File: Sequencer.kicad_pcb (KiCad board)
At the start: 4 copper layers, 100.6 x 100 mm, 230 parts, among them J1 Conn_02x03_Odd_Even, J2 Conn_02x05_Odd_Even, J3 Conn_02x03_Odd_Even, J4 Conn_01x03, Q1 BC847, Q2 BC847, Q3 BC847, Q4 BC847, SW1 SW_Push, SW10 SW_SPDT_MSM, SW11 SW_SPDT_MSM, SW12 SW_SPDT_MSM, SW2 SW_SPDT_MSM, SW3 SW_SPDT_MSM, SW4 SW_SPDT_MSM, SW5 SW_SPDT_MSM, SW6 SW_SPDT_MSM, SW7 SW_SPDT, SW8 SW_SPDT, SW9 SW_SPDT_MSM, U1 L7805, U10 TL072, U11 74AHCT1G125, U12 TL072, U13 74AHCT1G125, U14 TL072, U2 ATmega328PB-AU, U3 74AHCT1G125, U4 MCP6002-xMS, U5 MCP6002-xMS, U6 MCP6002-xMS, U7 MCP6002-xMS, U8 TL072, U9 74AHCT1G125, X1 20MHz

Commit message: Branding.
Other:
- board text added: "+12V"
- board text added: "-12V"
- board text added: "I2C"
- board text added: "ICSP"
- board text added: "Marangisto 2018"
- board text added: "Modular Sequencer"
- board text added: "Rev A"
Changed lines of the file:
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@@
   (general
     (thickness 1.6)
-    (drawings 88)
+    (drawings 96)
     (tracks 1658)
     (zones 0)
@@
     (descr "Through hole straight pin header, 2x03, 2.54mm pitch, double rows")
     (tags "Through hole pin header THT 2x03 2.54mm double row")
-    (fp_text reference J1 (at 1.27 2.33) (layer B.SilkS)
+    (fp_text reference J1 (at 1.26956 -7.36602) (layer B.SilkS)
       (effects (font (size 0.75 1) (thickness 0.15)) (justify mirror))
     )
@@
       (effects (font (size 0.75 1) (thickness 0.15)) (justify mirror))
     )
+    (fp_line (start 0 1.27) (end 3.81 1.27) (layer B.Fab) (width 0.1))
+    (fp_line (start 3.81 1.27) (end 3.81 -6.35) (layer B.Fab) (width 0.1))
+    (fp_line (start 3.81 -6.35) (end -1.27 -6.35) (layer B.Fab) (width 0.1))
+    (fp_line (start -1.27 -6.35) (end -1.27 0) (layer B.Fab) (width 0.1))
+    (fp_line (start -1.27 0) (end 0 1.27) (layer B.Fab) (width 0.1))
+    (fp_line (start -1.33 -6.41) (end 3.87 -6.41) (layer B.SilkS) (width 0.12))
+    (fp_line (start -1.33 -1.27) (end -1.33 -6.41) (layer B.SilkS) (width 0.12))
+    (fp_line (start 3.87 1.33) (end 3.87 -6.41) (layer B.SilkS) (width 0.12))
+    (fp_line (start -1.33 -1.27) (end 1.27 -1.27) (layer B.SilkS) (width 0.12))
+    (fp_line (start 1.27 -1.27) (end 1.27 1.33) (layer B.SilkS) (width 0.12))
+    (fp_line (start 1.27 1.33) (end 3.87 1.33) (layer B.SilkS) (width 0.12))
+    (fp_line (start -1.33 0) (end -1.33 1.33) (layer B.SilkS) (width 0.12))
+    (fp_line (start -1.33 1.33) (end 0 1.33) (layer B.SilkS) (width 0.12))
+    (fp_line (start -1.8 1.8) (end -1.8 -6.85) (layer B.CrtYd) (width 0.05))
+    (fp_line (start -1.8 -6.85) (end 4.35 -6.85) (layer B.CrtYd) (width 0.05))
+    (fp_line (start 4.35 -6.85) (end 4.35 1.8) (layer B.CrtYd) (width 0.05))
+    (fp_line (start 4.35 1.8) (end -1.8 1.8) (layer B.CrtYd) (width 0.05))
     (fp_text user %R (at 1.27 -2.54 -90) (layer B.Fab)
       (effects (font (size 1 1) (thickness 0.15)) (justify mirror))
     )
-    (fp_line (start 4.35 1.8) (end -1.8 1.8) (layer B.CrtYd) (width 0.05))
-    (fp_line (start 4.35 -6.85) (end 4.35 1.8) (layer B.CrtYd) (width 0.05))
-    (fp_line (start -1.8 -6.85) (end 4.35 -6.85) (layer B.CrtYd) (width 0.05))
-    (fp_line (start -1.8 1.8) (end -1.8 -6.85) (layer B.CrtYd) (width 0.05))
-    (fp_line (start -1.33 1.33) (end 0 1.33) (layer B.SilkS) (width 0.12))
-    (fp_line (start -1.33 0) (end -1.33 1.33) (layer B.SilkS) (width 0.12))
-    (fp_line (start 1.27 1.33) (end 3.87 1.33) (layer B.SilkS) (width 0.12))
-    (fp_line (start 1.27 -1.27) (end 1.27 1.33) (layer B.SilkS) (width 0.12))
-    (fp_line (start -1.33 -1.27) (end 1.27 -1.27) (layer B.SilkS) (width 0.12))
-    (fp_line (start 3.87 1.33) (end 3.87 -6.41) (layer B.SilkS) (width 0.12))
-    (fp_line (start -1.33 -1.27) (end -1.33 -6.41) (layer B.SilkS) (width 0.12))
-    (fp_line (start -1.33 -6.41) (end 3.87 -6.41) (layer B.SilkS) (width 0.12))
-    (fp_line (start -1.27 0) (end 0 1.27) (layer B.Fab) (width 0.1))
-    (fp_line (start -1.27 -6.35) (end -1.27 0) (layer B.Fab) (width 0.1))
-    (fp_line (start 3.81 -6.35) (end -1.27 -6.35) (layer B.Fab) (width 0.1))
-    (fp_line (start 3.81 1.27) (end 3.81 -6.35) (layer B.Fab) (width 0.1))
-    (fp_line (start 0 1.27) (end 3.81 1.27) (layer B.Fab) (width 0.1))
-    (pad 6 thru_hole oval (at 2.54 -5.08) (size 1.7 1.7) (drill 1) (layers *.Cu *.Mask)
-      (net 3 +5V))
-    (pad 5 thru_hole oval (at 0 -5.08) (size 1.7 1.7) (drill 1) (layers *.Cu *.Mask)
-      (net 3 +5V))
-    (pad 4 thru_hole oval (at 2.54 -2.54) (size 1.7 1.7) (drill 1) (layers *.Cu *.Mask)
-      (net 43 SCL))
-    (pad 3 thru_hole oval (at 0 -2.54) (size 1.7 1.7) (drill 1) (layers *.Cu *.Mask)
-      (net 42 SDA))
-    (pad 2 thru_hole oval (at 2.54 0) (size 1.7 1.7) (drill 1) (layers *.Cu *.Mask)
-      (net 149 GND))
     (pad 1 thru_hole rect (at 0 0) (size 1.7 1.7) (drill 1) (layers *.Cu *.Mask)
       (net 149 GND))
+    (pad 2 thru_hole oval (at 2.54 0) (size 1.7 1.7) (drill 1) (layers *.Cu *.Mask)
+      (net 149 GND))
+    (pad 3 thru_hole oval (at 0 -2.54) (size 1.7 1.7) (drill 1) (layers *.Cu *.Mask)
+      (net 42 SDA))
+    (pad 4 thru_hole oval (at 2.54 -2.54) (size 1.7 1.7) (drill 1) (layers *.Cu *.Mask)
+      (net 43 SCL))
+    (pad 5 thru_hole oval (at 0 -5.08) (size 1.7 1.7) (drill 1) (layers *.Cu *.Mask)
+      (net 3 +5V))
+    (pad 6 thru_hole oval (at 2.54 -5.08) (size 1.7 1.7) (drill 1) (layers *.Cu *.Mask)
+      (net 3 +5V))
     (model ${KISYS3DMOD}/Connector_PinHeader_2.54mm.3dshapes/PinHeader_2x03_P2.54mm_Vertical.wrl
       (at (xyz 0 0 0))
@@
     )
   )
+  (gr_text ICSP (at 157.64256 153.39568) (layer B.SilkS)
+    (effects (font (size 1 1.5) (thickness 0.2)) (justify mirror))
+  )
+  (gr_text I2C (at 118.14556 72.49668) (layer B.SilkS)
+    (effects (font (size 1 1.5) (thickness 0.2)) (justify mirror))
+  )
+  (gr_text "+12V\n\n" (at 184.05856 59.92368) (layer B.SilkS)
+    (effects (font (size 1 1) (thickness 0.25)) (justify mirror))
+  )
+  (gr_text "-12V\n\n" (at 173.89856 69.95668) (layer B.SilkS)
+    (effects (font (size 1 1) (thickness 0.25)) (justify mirror))
+  )
+  (gr_line (start 181.13756 71.22668) (end 176.81956 71.22668) (layer B.SilkS) (width 0.4))
+  (gr_text "Rev A" (at 196.63156 100.43668 90) (layer B.SilkS)
+    (effects (font (size 1.5 1.5) (thickness 0.3)) (justify mirror))
+  )
+  (gr_text "Marangisto 2018" (at 196.63156 66.52768 90) (layer B.SilkS)
+    (effects (font (size 1.5 1.5) (thickness 0.3)) (justify mirror))
+  )
+  (gr_text "Modular  Sequencer" (at 101.63556 87.86368 90) (layer B.SilkS)
+    (effects (font (size 4 3.5) (thickness 0.3)) (justify mirror))
+  )
   (gr_line (start 198.8011 155.0036) (end 198.8011 55.0036) (layer Edge.Cuts) (width 0.2))

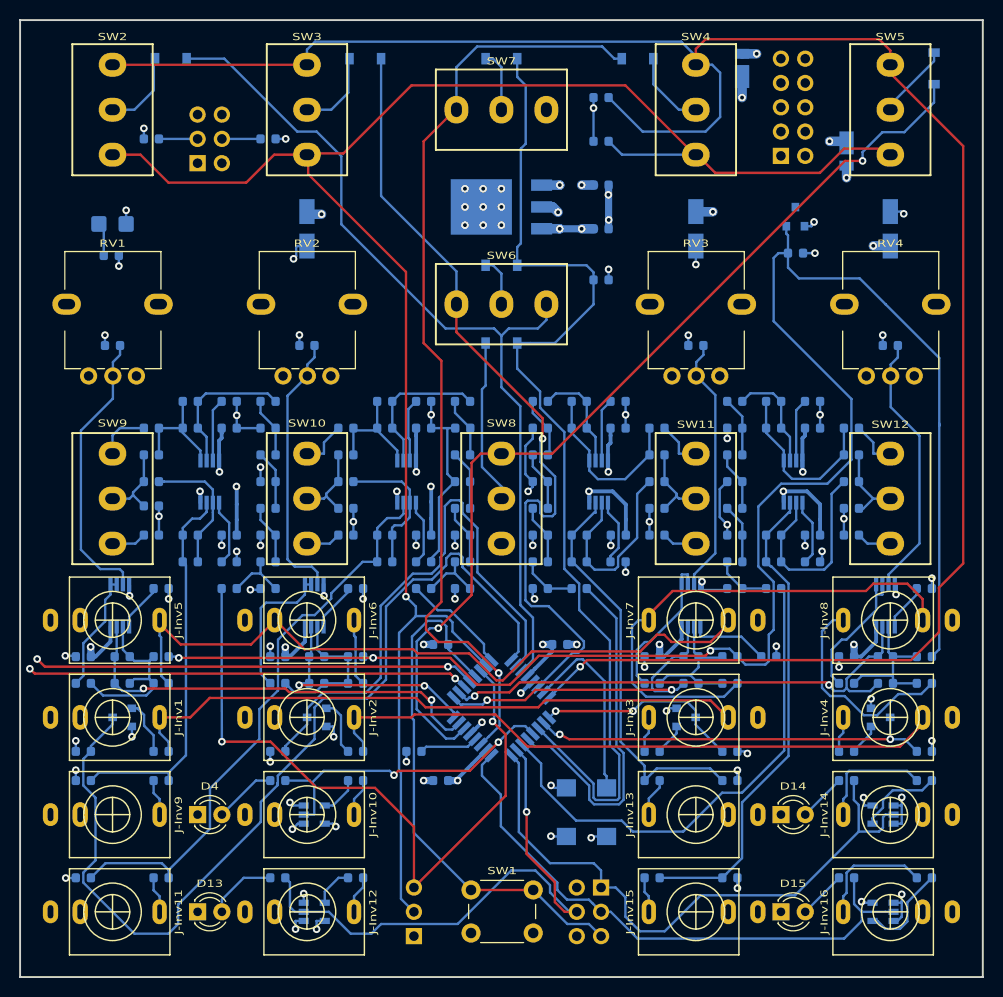
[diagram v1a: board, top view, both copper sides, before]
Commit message: Front ground-pour.
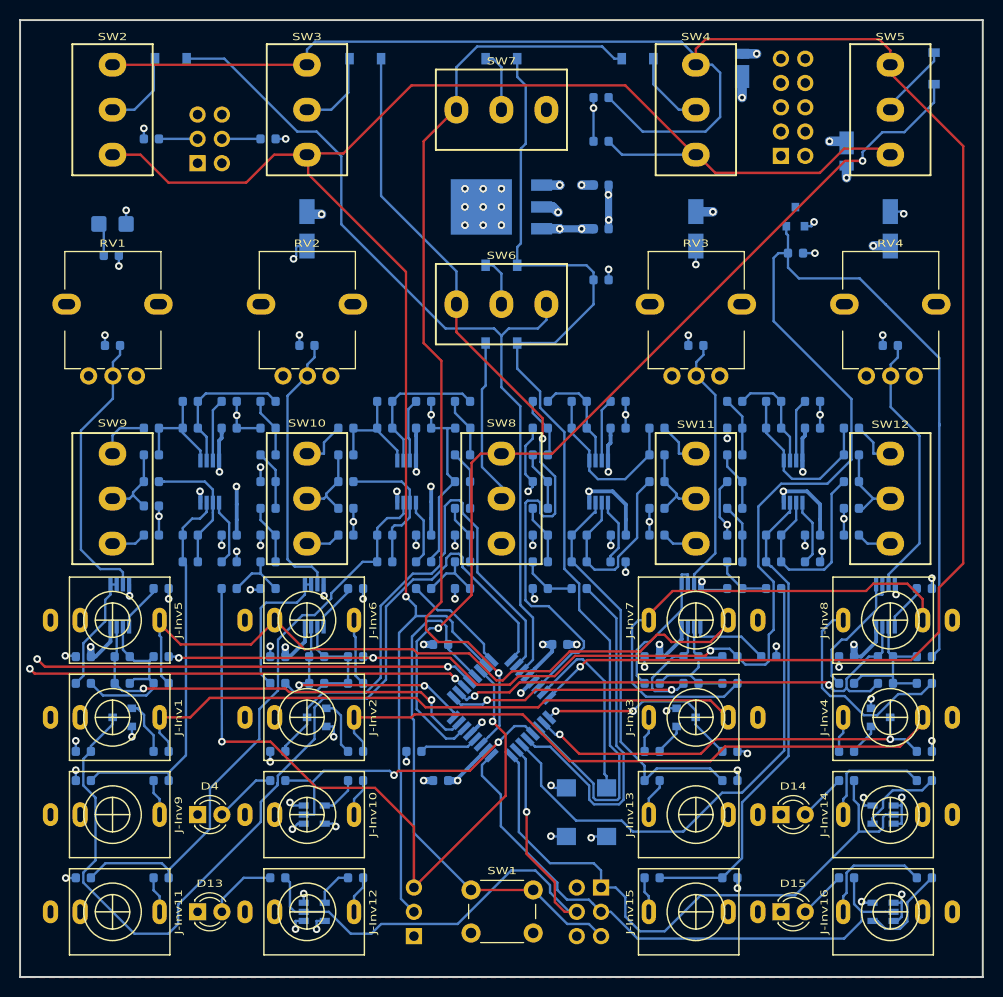
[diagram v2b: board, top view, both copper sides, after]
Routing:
- net RST1: track 42.4 -> 43.8 mm
- net /sheet5C188821/In: track 66.5 -> 67.8 mm
- added copper zone on F.Cu, net GND
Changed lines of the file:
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@@
     (thickness 1.6)
     (drawings 96)
-    (tracks 1658)
+    (tracks 1667)
     (zones 0)
     (modules 230)
@@
   (page A4)
   (layers
-    (0 F.Cu signal hide)
-    (1 In1.Cu power hide)
-    (2 In2.Cu power hide)
+    (0 F.Cu signal)
+    (1 In1.Cu power)
+    (2 In2.Cu power)
     (31 B.Cu signal)
     (32 B.Adhes user)
@@
     (35 F.Paste user)
     (36 B.SilkS user)
-    (37 F.SilkS user hide)
+    (37 F.SilkS user)
     (38 B.Mask user)
     (39 F.Mask user)
-    (40 Dwgs.User user hide)
+    (40 Dwgs.User user)
     (41 Cmts.User user)
     (42 Eco1.User user)
@@
     (44 Edge.Cuts user)
     (45 Margin user)
-    (46 B.CrtYd user hide)
-    (47 F.CrtYd user hide)
-    (48 B.Fab user hide)
-    (49 F.Fab user hide)
+    (46 B.CrtYd user)
+    (47 F.CrtYd user)
+    (48 B.Fab user)
+    (49 F.Fab user)
   )
   (setup
@@
     (user_trace_width 1)
     (trace_clearance 0.2)
-    (zone_clearance 0.762)
+    (zone_clearance 0.508)
     (zone_45_only no)
     (trace_min 0.2)
@@
   (segment (start 170.5524 120.697) (end 172.3405 120.697) (width 0.25) (layer B.Cu) (net 9))
   (segment (start 172.3405 120.697) (end 173.1625 121.519) (width 0.25) (layer B.Cu) (net 9))
-  (segment (start 170.343 120.9064) (end 169.8166 121.4328) (width 0.25) (layer F.Cu) (net 9))
-  (segment (start 169.8166 121.4328) (end 152.4098 121.4328) (width 0.25) (layer F.Cu) (net 9))
-  (segment (start 152.4098 121.4328) (end 149.3865 124.4561) (width 0.25) (layer F.Cu) (net 9))
-  (segment (start 149.3865 124.4561) (end 145.9607 124.4561) (width 0.25) (layer F.Cu) (net 9))
-  (segment (start 145.9607 124.4561) (end 143.154 121.6494) (width 0.25) (layer F.Cu) (net 9))
-  (segment (start 143.154 121.6494) (end 135.0936 121.6494) (width 0.25) (layer F.Cu) (net 9))
   (segment (start 135.0936 121.6494) (end 114.7827 121.6494) (width 0.25) (layer F.Cu) (net 9))
   (segment (start 113.7265 121.519) (end 114.6523 121.519) (width 0.25) (layer B.Cu) (net 9))
@@
   (segment (start 176.439 121.9985) (end 176.439 119.23224) (width 0.25) (layer B.Cu) (net 9))
   (segment (start 176.439 119.23224) (end 176.947 118.72424) (width 0.25) (layer B.Cu) (net 9))
+  (segment (start 145.9607 124.4561) (end 143.154 121.6494) (width 0.25) (layer F.Cu) (net 9))
+  (segment (start 169.8166 121.4328) (end 156.20444 121.4328) (width 0.25) (layer F.Cu) (net 9))
+  (segment (start 170.343 120.9064) (end 169.8166 121.4328) (width 0.25) (layer F.Cu) (net 9))
+  (segment (start 143.154 121.6494) (end 135.0936 121.6494) (width 0.25) (layer F.Cu) (net 9))
+  (segment (start 156.20444 121.4328) (end 154.0712 123.56604) (width 0.25) (layer F.Cu) (net 9))
+  (segment (start 149.3865 124.4561) (end 145.9607 124.4561) (width 0.25) (layer F.Cu) (net 9))
+  (segment (start 154.0712 123.56604) (end 150.27656 123.56604) (width 0.25) (layer F.Cu) (net 9))
+  (segment (start 150.27656 123.56604) (end 149.3865 124.4561) (width 0.25) (layer F.Cu) (net 9))
   (segment (start 128.4075 124.313) (end 127.5382 124.313) (width 0.25) (layer B.Cu) (net 10))
   (segment (start 127.5382 124.313) (end 127.3506 124.5006) (width 0.25) (layer B.Cu) (net 10))
@@
   (segment (start 190.63718 130.15468) (end 191.9075 131.425) (width 0.25) (layer B.Cu) (net 13))
   (segment (start 189.13856 130.15468) (end 190.63718 130.15468) (width 0.25) (layer B.Cu) (net 13))
-  (segment (start 154.59456 129.64668) (end 155.58538 130.15468) (width 0.25) (layer F.Cu) (net 13))
   (via (at 154.59456 129.64668) (size 0.8) (drill 0.4) (layers F.Cu B.Cu) (net 13))
-  (segment (start 155.58538 130.15468) (end 189.13856 130.15468) (width 0.25) (layer F.Cu) (net 13))
   (segment (start 154.12108 129.64668) (end 152.9184 128.444) (width 0.25) (layer B.Cu) (net 13))
   (segment (start 154.59456 129.64668) (end 154.12108 129.64668) (width 0.25) (layer B.Cu) (net 13))
+  (segment (start 156.62656 131.67868) (end 154.59456 129.64668) (width 0.25) (layer F.Cu) (net 13))
+  (segment (start 169.32656 131.67868) (end 156.62656 131.67868) (width 0.25) (layer F.Cu) (net 13))
+  (segment (start 189.13856 130.15468) (end 170.85056 130.15468) (width 0.25) (layer F.Cu) (net 13))
+  (segment (start 170.85056 130.15468) (end 169.32656 131.67868) (width 0.25) (layer F.Cu) (net 13))
   (segment (start 162.251 127.2125) (end 154.1683 127.2125) (width 0.25) (layer F.Cu) (net 14))
   (segment (start 153.4841 127.8783) (end 153.5025 127.8783) (width 0.25) (layer B.Cu) (net 14))
@@
   (segment (start 133.099 129.4943) (end 134.0465 130.4418) (width 0.25) (layer B.Cu) (net 64))
   (segment (start 134.0465 130.4418) (end 134.0465 131.425) (width 0.25) (layer B.Cu) (net 64))
-  (segment (start 192.519 128.55224) (end 190.15456 130.91668) (width 0.25) (layer F.Cu) (net 64))
-  (segment (start 151.22558 130.91668) (end 147.8768 127.5679) (width 0.25) (layer F.Cu) (net 64))
   (segment (start 139.10024 127.869) (end 133.099 127.869) (width 0.25) (layer F.Cu) (net 64))
-  (segment (start 192.519 127.869) (end 192.519 128.55224) (width 0.25) (layer F.Cu) (net 64))
-  (segment (start 190.15456 130.91668) (end 151.22558 130.91668) (width 0.25) (layer F.Cu) (net 64))
-  (segment (start 147.8768 127.5679) (end 139.40134 127.5679) (width 0.25) (layer F.Cu) (net 64))
   (segment (start 139.40134 127.5679) (end 139.10024 127.869) (width 0.25) (layer F.Cu) (net 64))
+  (segment (start 150.73778 127.5679) (end 139.40134 127.5679) (width 0.25) (layer F.Cu) (net 64))
+  (segment (start 192.519 127.869) (end 192.519 128.55224) (width 0.25) (layer F.Cu) (net 64))
+  (segment (start 192.519 128.55224) (end 190.15456 130.91668) (width 0.25) (layer F.Cu) (net 64))
+  (segment (start 190.15456 130.91668) (end 171.86656 130.91668) (width 0.25) (layer F.Cu) (net 64))
+  (segment (start 170.34256 132.44068) (end 155.61056 132.44068) (width 0.25) (layer F.Cu) (net 64))
+  (segment (start 171.86656 130.91668) (end 170.34256 132.44068) (width 0.25) (layer F.Cu) (net 64))
+  (segment (start 155.61056 132.44068) (end 150.73778 127.5679) (width 0.25) (layer F.Cu) (net 64))
   (segment (start 112.779 127.869) (end 112.779 129.4943) (width 0.25) (layer B.Cu) (net 65))
   (segment (start 112.779 129.4943) (end 113.7265 130.4418) (width 0.25) (layer B.Cu) (net 65))
@@
   (segment (start 147.9637 124.0057) (end 145.1433 121.1853) (width 0.25) (layer F.Cu) (net 133))
   (segment (start 148.6489 124.0057) (end 147.9637 124.0057) (width 0.25) (layer F.Cu) (net 133))
-  (segment (start 163.00474 120.9825) (end 151.6721 120.9825) (width 0.25) (layer F.Cu) (net 133))
   (segment (start 172.199 118.13824) (end 170.34256 119.99468) (width 0.25) (layer F.Cu) (net 133))
   (segment (start 172.199 117.709) (end 172.199 118.13824) (width 0.25) (layer F.Cu) (net 133))
-  (segment (start 151.6721 120.9825) (end 148.6489 124.0057) (width 0.25) (layer F.Cu) (net 133))
   (segment (start 165.51656 119.23268) (end 164.75456 119.23268) (width 0.25) (layer F.Cu) (net 133))
   (segment (start 145.1433 121.1853) (end 139.7282 121.1853) (width 0.25) (layer F.Cu) (net 133))
@@
   (segment (start 124.799 117.709) (end 124.799 117.78624) (width 0.25) (layer F.Cu) (net 133))
   (segment (start 124.799 117.78624) (end 122.33656 120.24868) (width 0.25) (layer F.Cu) (net 133))
+  (segment (start 155.61056 120.9825) (end 155.61056 121.01068) (width 0.25) (layer F.Cu) (net 133))
+  (segment (start 163.00474 120.9825) (end 155.61056 120.9825) (width 0.25) (layer F.Cu) (net 133))
+  (segment (start 153.57856 123.04268) (end 149.61192 123.04268) (width 0.25) (layer F.Cu) (net 133))
+  (segment (start 155.61056 121.01068) (end 153.57856 123.04268) (width 0.25) (layer F.Cu) (net 133))
+  (segment (start 149.61192 123.04268) (end 148.6489 124.0057) (width 0.25) (layer F.Cu) (net 133))
   (segment (start 109.596 118.385) (end 109.596 117.3347) (width 0.25) (layer B.Cu) (net 134))
   (segment (start 109.596 117.3347) (end 112.1515 114.7792) (width 0.25) (layer B.Cu) (net 134))
@@
     (min_thickness 0.254)
     (fill yes (arc_segments 16) (thermal_gap 0.508) (thermal_bridge_width 0.508))
+    (polygon
+      (pts
+        (xy 198.79056 54.97068) (xy 98.20656 54.97068) (xy 98.20656 155.04668) (xy 198.79056 155.04668)
+      )
+    )
+  )
+  (zone (net 149) (net_name GND) (layer F.Cu) (hatch edge 0.508)
+    (connect_pads (clearance 0.508))
+    (min_thickness 0.254)
+    (fill yes (arc_segments 16) (thermal_gap 0.508) (thermal_bridge_width 0.508))

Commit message: Back ground-pour.
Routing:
- net Scan1: track 85.0 -> 88.8 mm
- net Net-(C36-Pad1): track 60.8 -> 62.1 mm
- net Scan0: track 92.9 -> 94.3 mm
- net Net-(J3-Pad5): track 55.6 -> 56.9 mm
- net Sense2: track 108.3 -> 107.1 mm
- net Net-(D8-Pad2): track 8.22 -> 7.18 mm
- net Sense1: track 218.4 -> 219.2 mm
- net CLK0: track 101.3 -> 101.9 mm
- net GND: vias 78 -> 79
- added copper zone on B.Cu, net GND
